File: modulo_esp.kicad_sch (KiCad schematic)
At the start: 3 parts

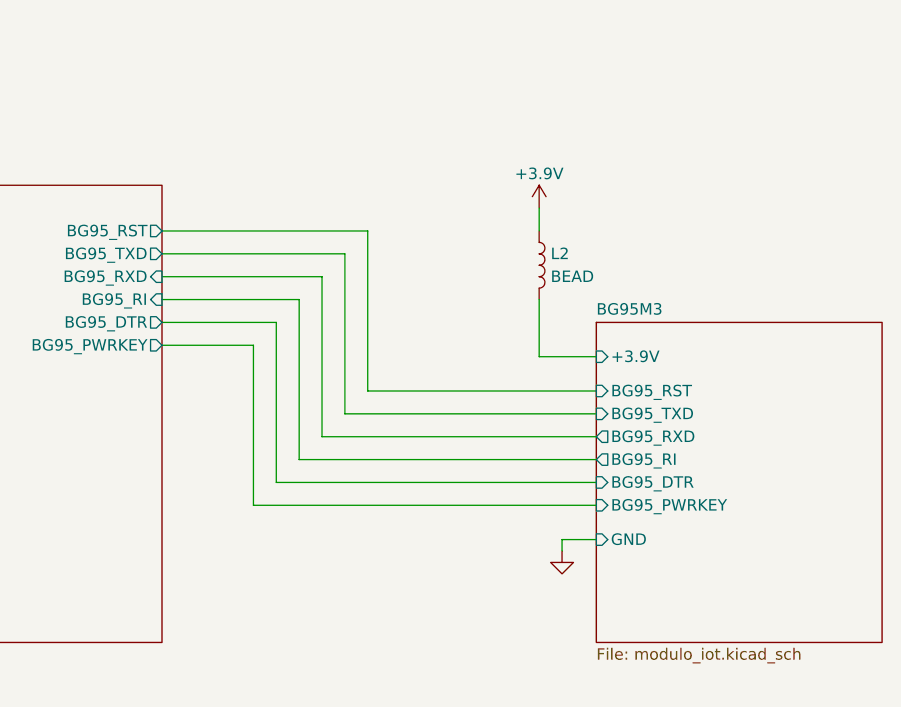
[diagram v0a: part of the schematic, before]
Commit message: Corrigido hierarchical label +3.3V do Módulo IoT
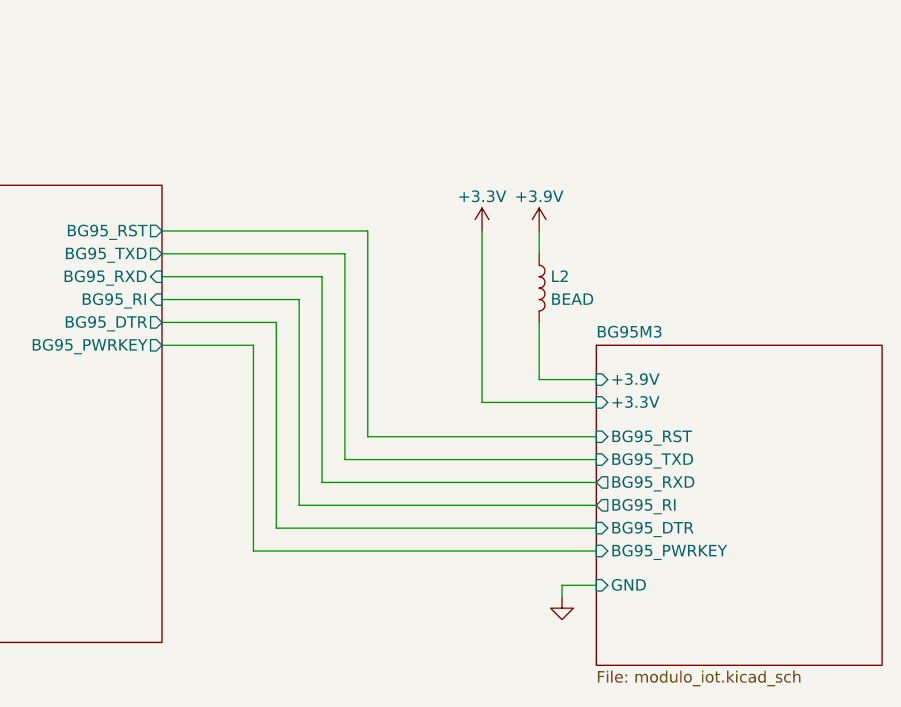
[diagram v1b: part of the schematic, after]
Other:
- sheet BG95M3 ports: added +3.3V; removed none
- moved on the sheet: L2

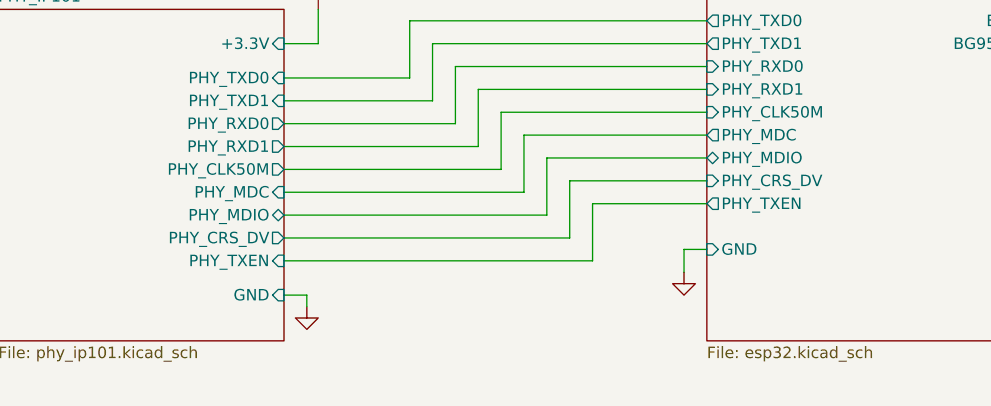
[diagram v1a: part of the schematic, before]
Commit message: Inserido um pino de controle de reset do PHY
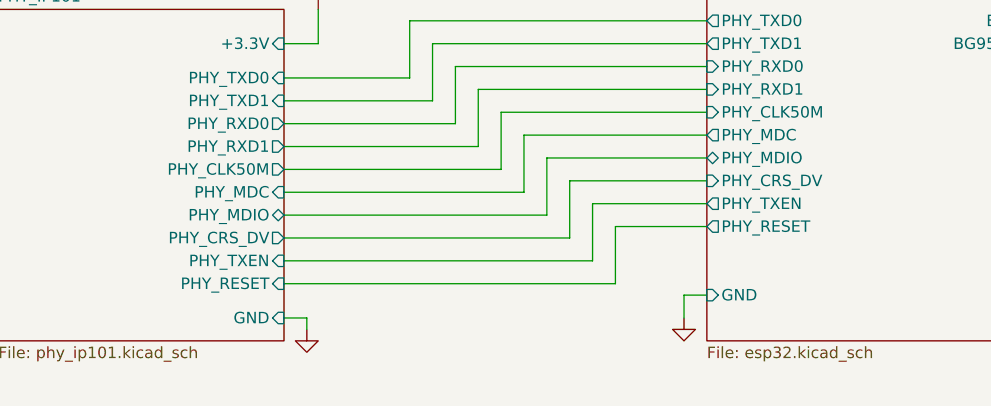
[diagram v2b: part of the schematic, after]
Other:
- sheet ESP32 ports: added PHY_RESET; removed none
- sheet PHY_IP101 ports: added PHY_RESET; removed none
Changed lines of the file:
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@@
+    (stroke (width 0) (type default) (color 0 0 0 0))
+  )
+  (wire (pts (xy 113.03 128.27) (xy 113.03 134.62))
     (stroke (width 0) (type default) (color 0 0 0 0))
   )
@@
     (stroke (width 0) (type default) (color 0 0 0 0))
   )
-  (wire (pts (xy 78.74 135.89) (xy 78.74 137.16))
+  (wire (pts (xy 78.74 138.43) (xy 78.74 139.7))
     (stroke (width 0) (type default) (color 0 0 0 0))
   )
@@
     (stroke (width 0) (type default) (color 0 0 0 0))
   )
+  (wire (pts (xy 123.19 128.27) (xy 113.03 128.27))
+    (stroke (width 0) (type default) (color 0 0 0 0))
+  )
   (wire (pts (xy 107.95 129.54) (xy 107.95 123.19))
     (stroke (width 0) (type default) (color 0 0 0 0))
@@
     (stroke (width 0) (type default) (color 0 0 0 0))
   )
-  (wire (pts (xy 120.65 130.81) (xy 120.65 133.35))
+  (wire (pts (xy 120.65 135.89) (xy 120.65 138.43))
     (stroke (width 0) (type default) (color 0 0 0 0))
   )
@@
     (stroke (width 0) (type default) (color 0 0 0 0))
   )
+  (wire (pts (xy 113.03 134.62) (xy 76.2 134.62))
+    (stroke (width 0) (type default) (color 0 0 0 0))
+  )
   (wire (pts (xy 110.49 125.73) (xy 123.19 125.73))
     (stroke (width 0) (type default) (color 0 0 0 0))
@@
     (stroke (width 0) (type default) (color 0 0 0 0))
   )
-  (wire (pts (xy 123.19 130.81) (xy 120.65 130.81))
+  (wire (pts (xy 123.19 135.89) (xy 120.65 135.89))
     (stroke (width 0) (type default) (color 0 0 0 0))
   )
@@
     (stroke (width 0) (type default) (color 0 0 0 0))
   )
-  (wire (pts (xy 76.2 135.89) (xy 78.74 135.89))
+  (wire (pts (xy 76.2 138.43) (xy 78.74 138.43))
     (stroke (width 0) (type default) (color 0 0 0 0))
   )
@@
     (pin "1")
   )
-  (symbol (lib_id "power:GND") (at 120.65 133.35 0) (unit 1)
+  (symbol (lib_id "power:GND") (at 120.65 138.43 0) (unit 1)
     (in_bom yes) (on_board yes) (fields_autoplaced)
-    (property "Reference" "#PWR010" (id 0) (at 120.65 139.7 0)
-      (effects (font (size 1.27 1.27)) hide)
-    )
-    (property "Value" "GND" (id 1) (at 120.65 138.43 0)
-      (effects (font (size 1.27 1.27)) hide)
-    )
-    (property "Footprint" "" (id 2) (at 120.65 133.35 0)
-      (effects (font (size 1.27 1.27)) hide)
-    )
-    (property "Datasheet" "" (id 3) (at 120.65 133.35 0)
+    (property "Reference" "#PWR010" (id 0) (at 120.65 144.78 0)
+      (effects (font (size 1.27 1.27)) hide)
+    )
+    (property "Value" "GND" (id 1) (at 120.65 143.51 0)
+      (effects (font (size 1.27 1.27)) hide)
+    )
+    (property "Footprint" "" (id 2) (at 120.65 138.43 0)
+      (effects (font (size 1.27 1.27)) hide)
+    )
+    (property "Datasheet" "" (id 3) (at 120.65 138.43 0)
       (effects (font (size 1.27 1.27)) hide)
     )
@@
     (pin "1")
   )
-  (symbol (lib_id "power:GND") (at 78.74 137.16 0) (unit 1)
+  (symbol (lib_id "power:GND") (at 78.74 139.7 0) (unit 1)
     (in_bom yes) (on_board yes) (fields_autoplaced)
-    (property "Reference" "#PWR011" (id 0) (at 78.74 143.51 0)
-      (effects (font (size 1.27 1.27)) hide)
-    )
-    (property "Value" "GND" (id 1) (at 78.74 142.24 0)
-      (effects (font (size 1.27 1.27)) hide)
-    )
-    (property "Footprint" "" (id 2) (at 78.74 137.16 0)
-      (effects (font (size 1.27 1.27)) hide)
-    )
-    (property "Datasheet" "" (id 3) (at 78.74 137.16 0)
+    (property "Reference" "#PWR011" (id 0) (at 78.74 146.05 0)
+      (effects (font (size 1.27 1.27)) hide)
+    )
+    (property "Value" "GND" (id 1) (at 78.74 144.78 0)
+      (effects (font (size 1.27 1.27)) hide)
+    )
+    (property "Footprint" "" (id 2) (at 78.74 139.7 0)
+      (effects (font (size 1.27 1.27)) hide)
+    )
+    (property "Datasheet" "" (id 3) (at 78.74 139.7 0)
       (effects (font (size 1.27 1.27)) hide)
     )
@@
       (effects (font (size 1.27 1.27)) (justify right))
     )
-    (pin "GND" input (at 76.2 135.89 0)
+    (pin "GND" input (at 76.2 138.43 0)
       (effects (font (size 1.27 1.27)) (justify right))
     )
@@
     )
     (pin "PHY_TXEN" input (at 76.2 132.08 0)
+      (effects (font (size 1.27 1.27)) (justify right))
+    )
+    (pin "PHY_RESET" input (at 76.2 134.62 0)
       (effects (font (size 1.27 1.27)) (justify right))
     )
@@
       (effects (font (size 1.27 1.27)) (justify left))
     )
-    (pin "GND" input (at 123.19 130.81 180)
+    (pin "GND" input (at 123.19 135.89 180)
       (effects (font (size 1.27 1.27)) (justify left))
     )
@@
     )
     (pin "VCC" input (at 123.19 95.25 180)
+      (effects (font (size 1.27 1.27)) (justify left))
+    )
+    (pin "PHY_RESET" output (at 123.19 128.27 180)
       (effects (font (size 1.27 1.27)) (justify left))
     )
@@
       (reference "R86") (unit 1) (value "100k") (footprint "Resistor_SMD:R_0603_1608Metric_Pad0.98x0.95mm_HandSolder")
     )
+    (path "/7b11f4fb-9ca5-474d-979f-5c95c69d797c/affa8a04-2416-456b-b47d-3fae28b4b1f9"
+      (reference "R?") (unit 1) (value "0R") (footprint "Resistor_SMD:R_0603_1608Metric_Pad0.98x0.95mm_HandSolder")
+    )
+    (path "/fad468d2-9036-4024-8b69-088056b4a2a2/f575f951-b4fb-4ed6-a41e-4cf1b0ca8d19"
+      (reference "R?") (unit 1) (value "0R") (footprint "Resistor_SMD:R_0603_1608Metric_Pad0.98x0.95mm_HandSolder")
+    )
     (path "/fad468d2-9036-4024-8b69-088056b4a2a2/7e066626-dc6e-4d13-b43a-a0d98d7fb577"

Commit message: Referencia dos componentes
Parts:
- renumbered L3 to L2, L2 to L3

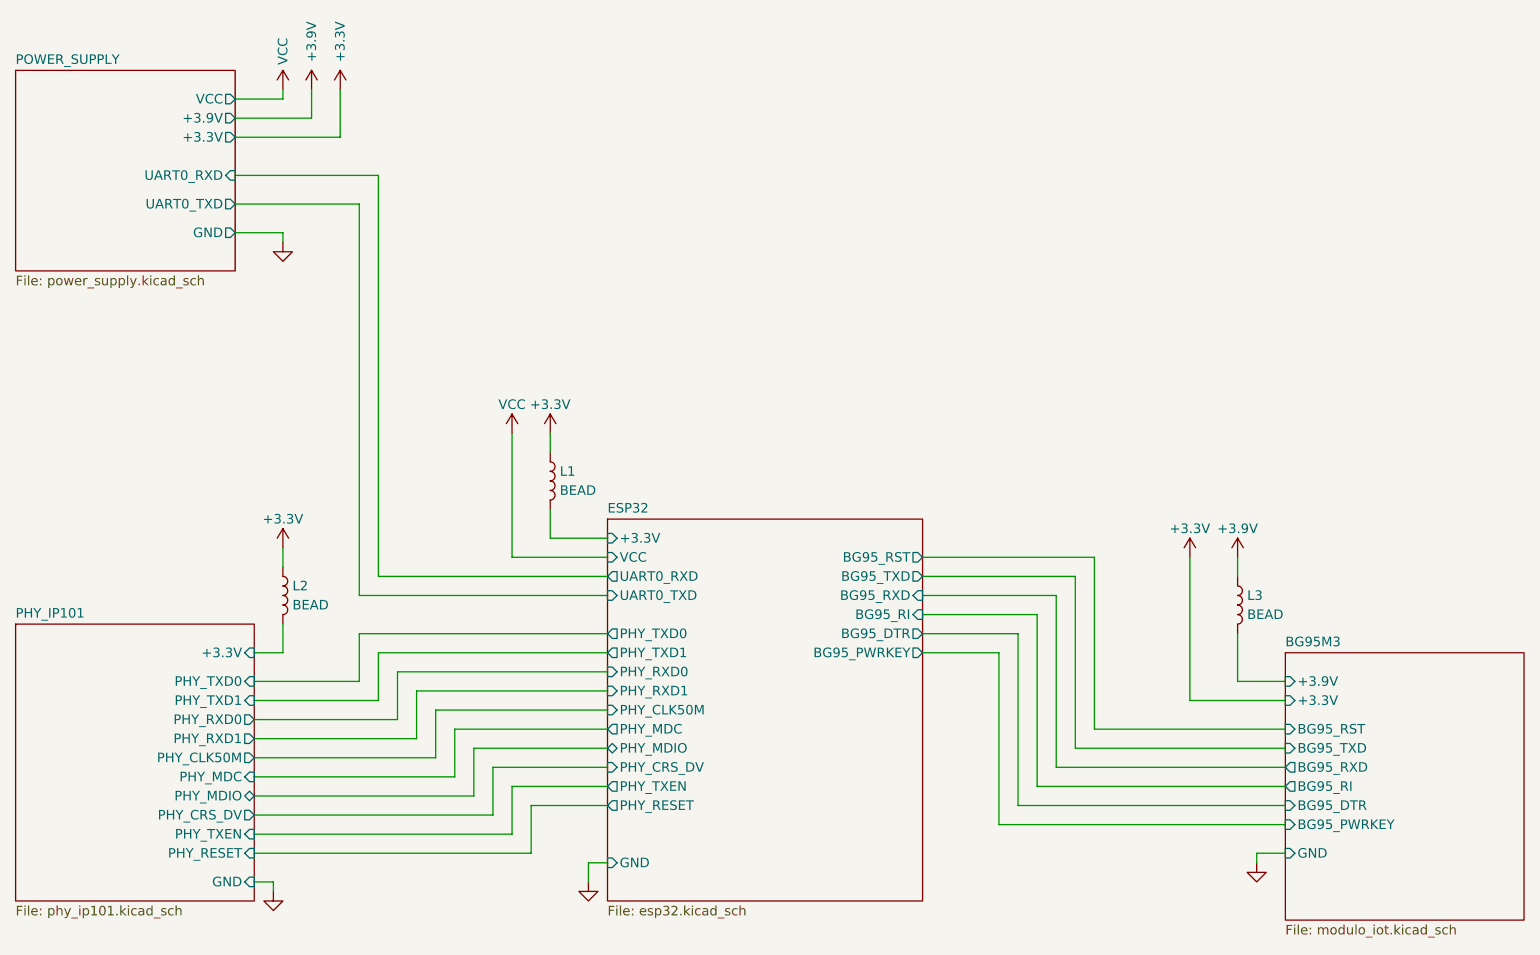
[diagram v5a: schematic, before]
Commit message: Adicionado os pads dos Test Point e alterado o Bead
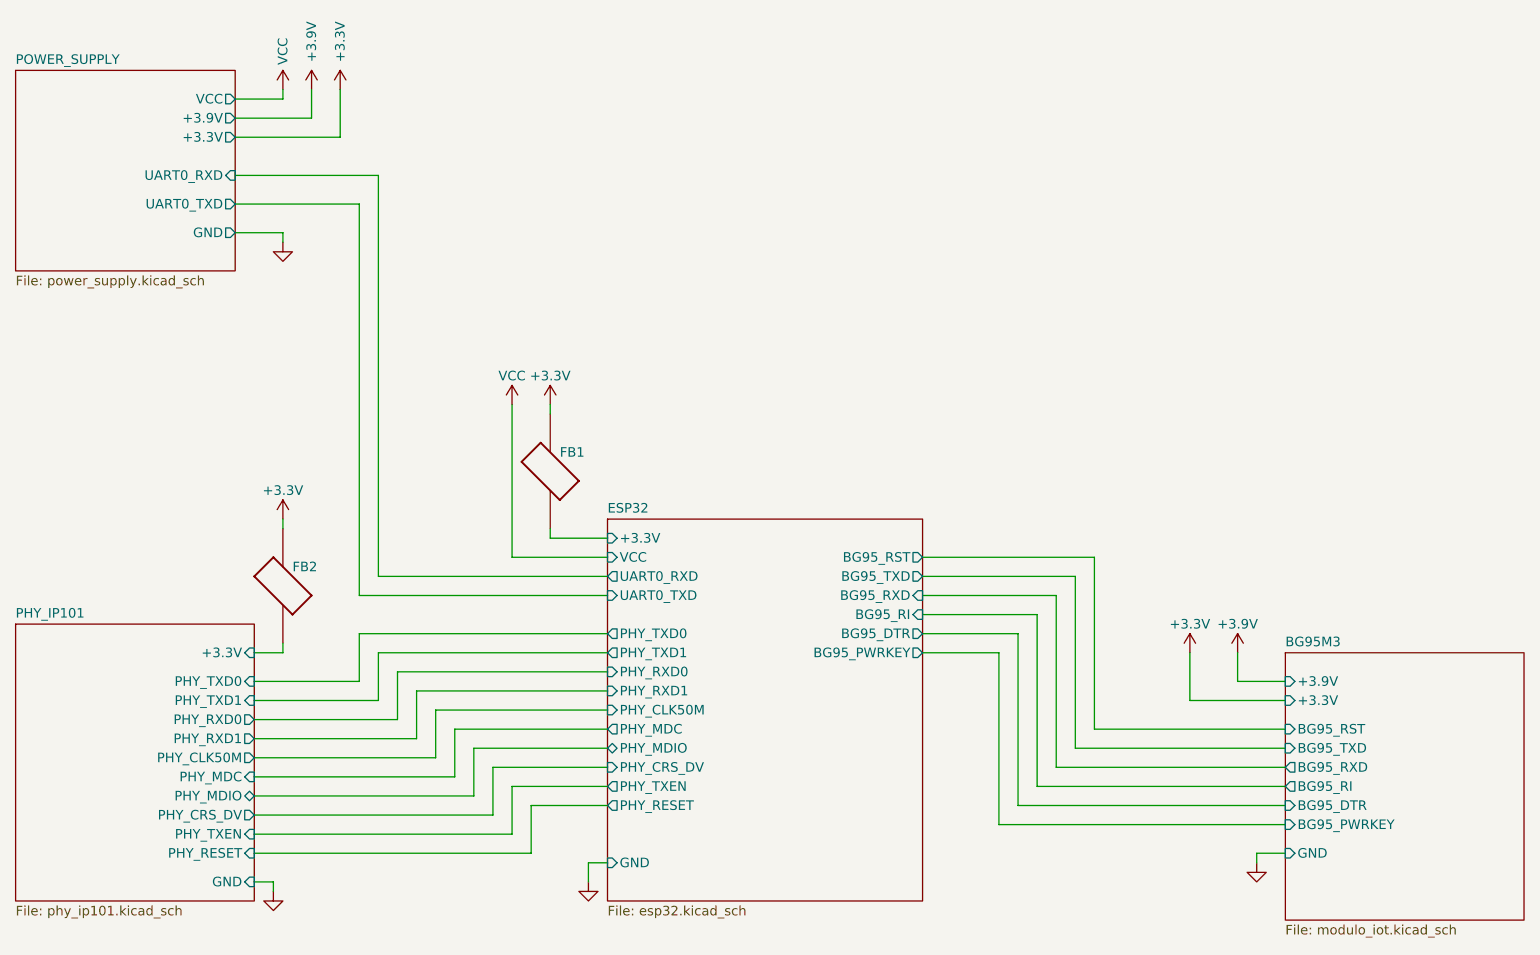
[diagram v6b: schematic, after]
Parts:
- removed L1, L2, L3: BEAD, Inductor_SMD:L_0603_1608Metric_Pad1.05x0.95mm_HandSolder, symbol Device:L
- added FB1: MPZ2012S102AT000, Alexandre_Library:BEADC2012X105N, symbol Alexandre_Library:MPZ2012S102AT000
- added FB2: (no value), symbol Alexandre_Library:MPZ2012S102AT000
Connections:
- net +3V3: now also FB1.2, FB2.2
- net ESP32/+3.3V: now also FB1.1
- net PHY_IP101/+3.3V: now also FB2.1

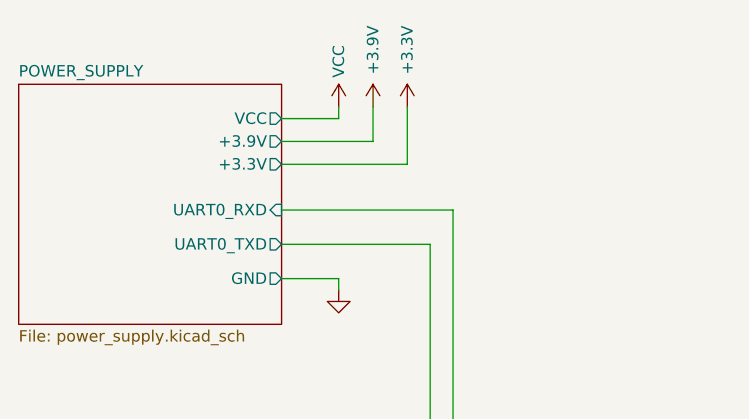
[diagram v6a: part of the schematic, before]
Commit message: Iniciando a posicionar os componentes no PCB
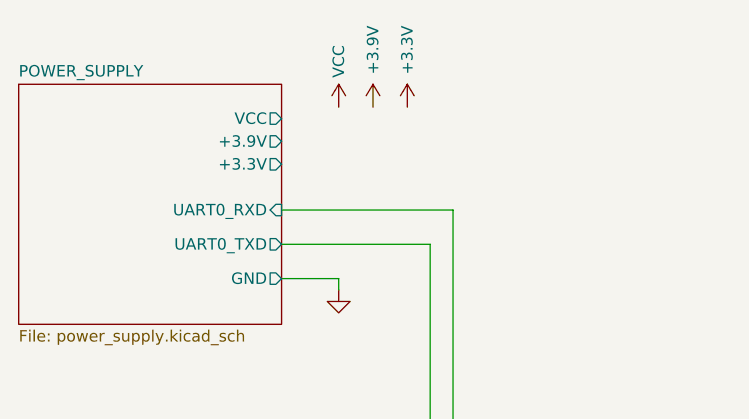
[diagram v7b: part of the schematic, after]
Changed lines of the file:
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@@
-    (stroke (width 0) (type default) (color 0 0 0 0))
-  )
-  (wire (pts (xy 73.66 34.29) (xy 80.01 34.29))
     (stroke (width 0) (type default) (color 0 0 0 0))
   )
@@
     (stroke (width 0) (type default) (color 0 0 0 0))
   )
-  (wire (pts (xy 87.63 33.02) (xy 87.63 39.37))
-    (stroke (width 0) (type default) (color 0 0 0 0))
-  )
   (wire (pts (xy 97.79 113.03) (xy 123.19 113.03))
     (stroke (width 0) (type default) (color 0 0 0 0))
@@
     (stroke (width 0) (type default) (color 0 0 0 0))
   )
-  (wire (pts (xy 73.66 36.83) (xy 83.82 36.83))
-    (stroke (width 0) (type default) (color 0 0 0 0))
-  )
   (wire (pts (xy 165.1 107.95) (xy 175.26 107.95))
     (stroke (width 0) (type default) (color 0 0 0 0))
@@
     (stroke (width 0) (type default) (color 0 0 0 0))
   )
-  (wire (pts (xy 80.01 34.29) (xy 80.01 33.02))
-    (stroke (width 0) (type default) (color 0 0 0 0))
-  )
-  (wire (pts (xy 83.82 33.02) (xy 83.82 36.83))
-    (stroke (width 0) (type default) (color 0 0 0 0))
-  )
   (wire (pts (xy 90.17 105.41) (xy 90.17 111.76))
     (stroke (width 0) (type default) (color 0 0 0 0))
@@
   )
   (wire (pts (xy 102.87 124.46) (xy 102.87 118.11))
-    (stroke (width 0) (type default) (color 0 0 0 0))
-  )
-  (wire (pts (xy 87.63 39.37) (xy 73.66 39.37))
     (stroke (width 0) (type default) (color 0 0 0 0))
   )
@@
       (reference "#PWR017") (unit 1) (value "GND") (footprint "")
     )
-    (path "/32e232d5-57bb-46e3-a8e5-df7ec6f170f8/c3723f71-89fb-4657-b366-397fe19ac7a2"
-      (reference "#PWR18") (unit 1) (value "+3.9V") (footprint "")
-    )
-    (path "/32e232d5-57bb-46e3-a8e5-df7ec6f170f8/76ad7656-07ba-4d43-bc0d-1453d3768625"
-      (reference "#PWR019") (unit 1) (value "+3.3V") (footprint "")
-    )
     (path "/32e232d5-57bb-46e3-a8e5-df7ec6f170f8/20ec1326-09e7-4d08-9114-d3d5b092c248"
       (reference "#PWR020") (unit 1) (value "VBUS") (footprint "")
@@
       (reference "#PWR035") (unit 1) (value "+5VD") (footprint "")
     )
-    (path "/32e232d5-57bb-46e3-a8e5-df7ec6f170f8/51dc3918-4b86-4df1-afb5-9fd4b1e1212e"
-      (reference "#PWR036") (unit 1) (value "+12V") (footprint "")
-    )
     (path "/32e232d5-57bb-46e3-a8e5-df7ec6f170f8/bc71f5ce-f2cd-4baa-8c06-92c183b12e3b"
       (reference "#PWR037") (unit 1) (value "VCC") (footprint "")
@@
       (reference "#PWR0108") (unit 1) (value "GND") (footprint "")
     )
+    (path "/32e232d5-57bb-46e3-a8e5-df7ec6f170f8/498fbcec-55c3-4a3e-8ecd-fc6dc2014399"
+      (reference "#PWR0109") (unit 1) (value "+12V") (footprint "")
+    )
     (path "/42a2b2c3-5ebb-49d9-aedb-3a59eff4693b/312cc4b0-8249-480e-bf7f-ea84576cfed6/ce3f3388-5de0-4595-b644-018e1029708b"
       (reference "#PWR109") (unit 1) (value "VDD_EXT") (footprint "")
     )
+    (path "/32e232d5-57bb-46e3-a8e5-df7ec6f170f8/c8316fa7-f307-43e6-a262-a7fc6200a6e3"
+      (reference "#PWR0110") (unit 1) (value "+3.3V") (footprint "")
+    )
     (path "/42a2b2c3-5ebb-49d9-aedb-3a59eff4693b/312cc4b0-8249-480e-bf7f-ea84576cfed6/d820a8c2-7491-4658-9ede-f566bfada3c0"
       (reference "#PWR110") (unit 1) (value "VDD_EXT") (footprint "")
@@
       (reference "#PWR111") (unit 1) (value "+3.3V") (footprint "")
     )
+    (path "/32e232d5-57bb-46e3-a8e5-df7ec6f170f8/dc7d61ef-0a5c-4007-8833-fa22a46837ce"
+      (reference "#PWR0111") (unit 1) (value "GND") (footprint "")
+    )
     (path "/42a2b2c3-5ebb-49d9-aedb-3a59eff4693b/312cc4b0-8249-480e-bf7f-ea84576cfed6/0ebcac5e-71ee-4229-89fc-e818dd9d5adc"
       (reference "#PWR112") (unit 1) (value "+3.3V") (footprint "")
@@
       (reference "TP1") (unit 1) (value "TestPoint") (footprint "TestPoint:TestPoint_Pad_1.5x1.5mm")
     )
-    (path "/32e232d5-57bb-46e3-a8e5-df7ec6f170f8/a5e8e95f-9e17-4eec-80b9-82a0e12dc841"
+    (path "/32e232d5-57bb-46e3-a8e5-df7ec6f170f8/247e79a9-3e9b-455d-904a-2a47264b37f9"
       (reference "TP2") (unit 1) (value "TestPoint") (footprint "TestPoint:TestPoint_Pad_1.5x1.5mm")
     )

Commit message: Continuando com o desenvolvimento do layout
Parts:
- FB2: value (none) -> MPZ2012S102AT000; footprint (none) -> Alexandre_Library:BEADC2012X105N
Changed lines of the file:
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@@
       (effects (font (size 1.27 1.27)) (justify right))
     )
-    (property "Value" "" (id 1) (at 74.93 86.36 0)
+    (property "Value" "MPZ2012S102AT000" (id 1) (at 74.93 86.36 0)
       (effects (font (size 1.27 1.27)) (justify right) hide)
     )
-    (property "Footprint" "" (id 2) (at 80.01 99.06 0)
+    (property "Footprint" "Alexandre_Library:BEADC2012X105N" (id 2) (at 80.01 99.06 0)
       (effects (font (size 1.27 1.27)) (justify left bottom) hide)
     )
